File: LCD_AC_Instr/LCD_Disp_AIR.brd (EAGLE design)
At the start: 40.3 x 49.5 mm, 12 parts, among them J1 CON_HEADER_1X02-PTH, SW1 ENCODER_SW1-PEC12

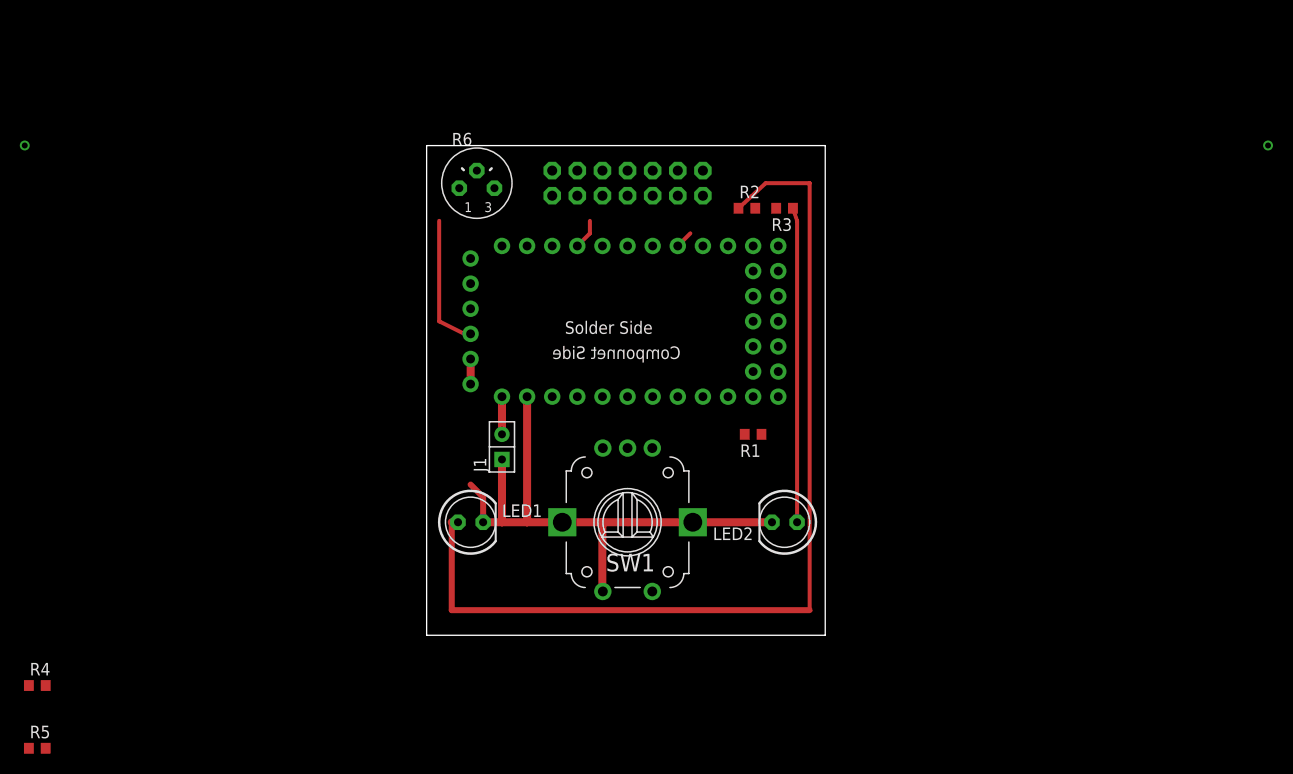
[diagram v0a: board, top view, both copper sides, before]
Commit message: finished design of PCB and uploaded to OSH PCB
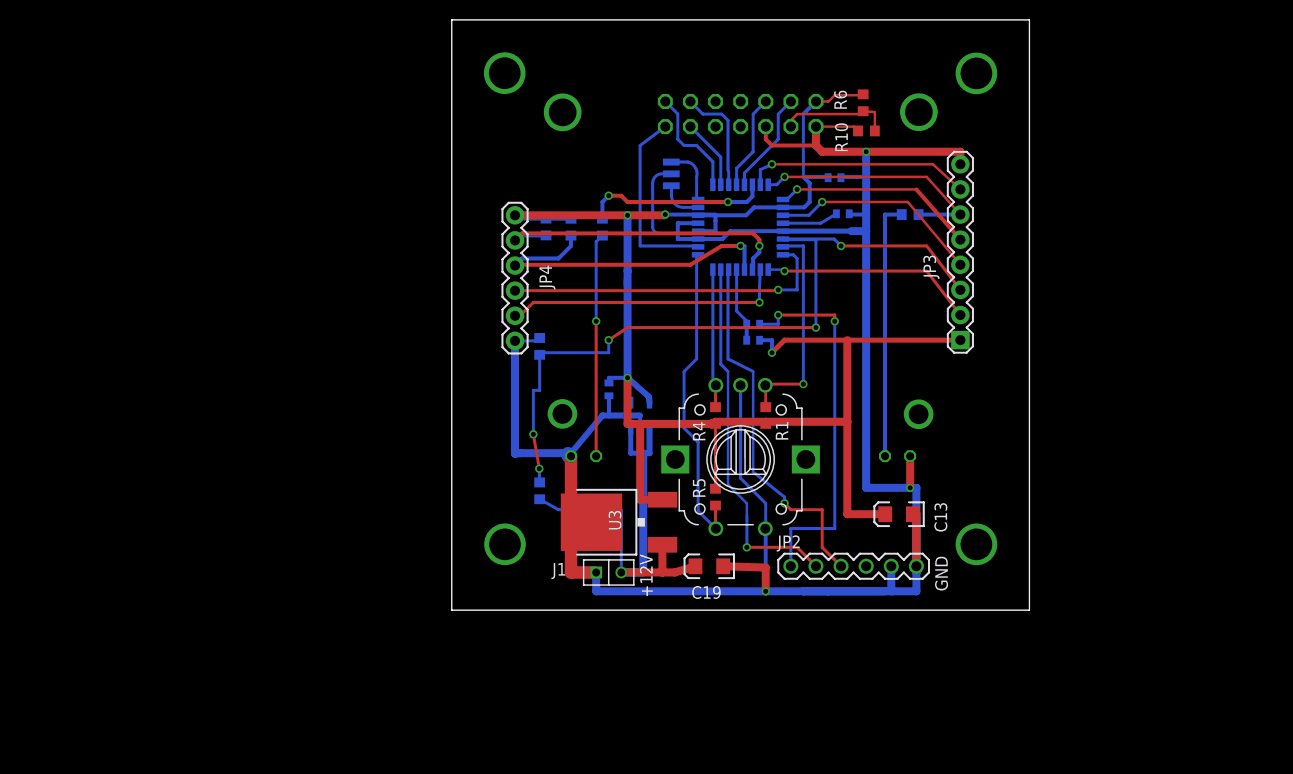
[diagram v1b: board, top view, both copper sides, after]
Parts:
- removed JP1: (no value), pinhead:2X07
- removed U$1: ARDUINO_PRO_MONI_DEEK_ROBOT, Arduino_Pro_FP:DEEK_ARDUINO_PR_MINI
- added C1, C10, C2, C3: 0.1uF, SparkFun:C0402
- added C13, C19: 10uF, SparkFun:EIA3216
- added JP2: 5V UART, SparkFun:1X06
- added JP3: 1, SparkFun-Connectors:1X08
- added JP4: 1, SparkFun-Connectors:1X06
- added LCD: LCD, pinhead:2X07
- added Q1: 16MHz, SparkFun:RESONATOR-SMD
- added R10, R11: 10K, dp_devices:R603
- added R12: 5K, dp_devices:R603
- added R7, R8: 1k, dp_devices:R603
- added R9: 10K, SparkFun:C0402
- added U1: ATMEGA328P, SparkFun:TQFP32-08
- added U2: 5V, SparkFun:SOT23-5
- added U3: +5V, wifi_WX:DPACK
- J1: value CON_HEADER_1X02-PTH -> 12V input
- R6: value (none) -> 10K; device pot:RJ6 -> dp_devices:R603
- moved R4 73.8 mm to (29.2, 21.0), turned to 90 degrees
- moved R5 73.1 mm to (29.2, 12.7), turned to 90 degrees
- moved R6 39.9 mm to (44.1, 52.6), turned to 90 degrees
- moved J1 16.7 mm to (18.4, 5.08), turned to 0 degrees
- moved R2 14.7 mm to (17.8, 40.0), flipped to the bottom, turned to 90 degrees
- moved LED1 13.2 mm to (15.9, 16.8), flipped to the bottom
- moved LED2 13.2 mm to (47.6, 16.8), flipped to the bottom
- moved SW1 13.1 mm to (31.8, 16.5)
- moved R3 12.7 mm to (48.9, 41.3), flipped to the bottom
- moved R1 2.29 mm to (34.3, 21.0), turned to 270 degrees
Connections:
- removed net +12V: J1.2, U$1.RAW
- removed net CONTRAST: JP1.3, R6.S
- removed net N$1: JP1.11, U$1.4
- removed net N$10: R4.2, SW1.A, U$1.2
- removed net N$11: U$1.A3
- removed net N$12: U$1.A0
- removed net N$3: JP1.12, U$1.5
- removed net N$4: JP1.6, U$1.9
- removed net N$7: R1.1, SW1.B, U$1.10
- removed net VCC_5V: JP1.2, R1.2, R4.1, R5.2, R6.E, U$1.VCC_2
- new net 12V_INPUT: C19.A, J1.2, R11.2, U2.1, U2.3, U3.1
- new net 5V: C10.1, C13.A, C3.2, JP3.1, JP4.1, LCD.2, R1.2, R4.1, R5.2, R6.2, R7.1, R8.1, R9.2, U1.18, U1.4, U1.6, U2.5, U3.3
- new net A0_PC0: R1.1, SW1.A, U1.23
- new net A1_PC1: JP4.4, U1.24
- new net A2_PC2: JP3.2, U1.25
- new net A3_PC3: JP4.5, U1.26
- new net A4_PC4: JP4.2, R7.2, U1.27
- new net A5_PC5: JP4.3, R8.2, U1.28
- new net ADC6: JP3.4, U1.19
- new net ADC7: JP3.3, R11.1, R12.2, U1.22
- new net AREF: C1.2, U1.20
- new net D10_PB2: R2.2, U1.14
- new net D11_PB3_MOSI: JP3.7, U1.15
- new net D12_PB4_MISO: JP3.6, R3.2, U1.16
- new net D13_PB5_SCK: JP3.5, U1.17
- new net D2_PD2: R4.2, SW1.B, U1.32
- new net D3_PD3: R5.1, SW1.P2, U1.1
- new net D4_PD4: LCD.13, U1.2
- new net D5_PD5: LCD.14, U1.9
- new net D6_PD6: LCD.11, U1.10
- new net D7_PD7: LCD.12, U1.11
- new net D8_PB0: LCD.6, U1.12
- new net D9_PB1: LCD.4, U1.13
- new net RESET: C2.1, R9.1, U1.29
- new net RXI: JP2.3, U1.30
- new net TXO: JP2.2, U1.31
- net GND: now also C1.1, C10.2, C13.C, C19.C, C3.1, JP2.5, JP2.6, JP3.8, JP4.6, LCD.1, LCD.5, Q1.2, R10.1, R12.1, SW1.P1, U1.21, U1.3, U1.5, U2.2, U3.4; no longer JP1.1, JP1.5, R6.A, SW1.P2, U$1.GND, U$1.GND_2, U$1.GND_3, U$1.GND_4
- net N$2: now also LCD.3, R10.2, R6.1; no longer JP1.13, U$1.6
- net N$5: now also Q1.1, U1.8; no longer JP1.4, U$1.8
- net N$6: now also C2.2, JP2.1; no longer R5.1, SW1.P1, U$1.3
- net N$9: now also Q1.3, U1.7; no longer JP1.14, U$1.7
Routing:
- net GND: track 65.2 -> 247.9 mm, vias 0 -> 3
- net 5V: track 0.00 -> 171.4 mm, vias 0 -> 4
- net ADC7: track 0.00 -> 76.1 mm, vias 0 -> 5
- net N$13: track 97.1 -> 22.6 mm, vias 0 -> 1
- net 12V_INPUT: track 0.00 -> 46.5 mm
- net N$6: track 0.00 -> 38.9 mm, vias 0 -> 2
- net RXI: track 0.00 -> 37.4 mm, vias 0 -> 1
- net TXO: track 0.00 -> 37.0 mm, vias 0 -> 1
- net A5_PC5: track 0.00 -> 33.9 mm, vias 0 -> 1
- net A1_PC1: track 0.00 -> 33.3 mm, vias 0 -> 1
- net D3_PD3: track 0.00 -> 32.1 mm
- net A4_PC4: track 0.00 -> 31.9 mm, vias 0 -> 1
- net A3_PC3: track 0.00 -> 28.6 mm, vias 0 -> 1
- net D12_PB4_MISO: track 0.00 -> 25.7 mm, vias 0 -> 1
- net A0_PC0: track 0.00 -> 22.9 mm, vias 0 -> 1
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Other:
- board size 40.3 x 49.5 mm -> 58.4 x 59.7 mm
- board text added: "+12V"
- board text added: "GND"

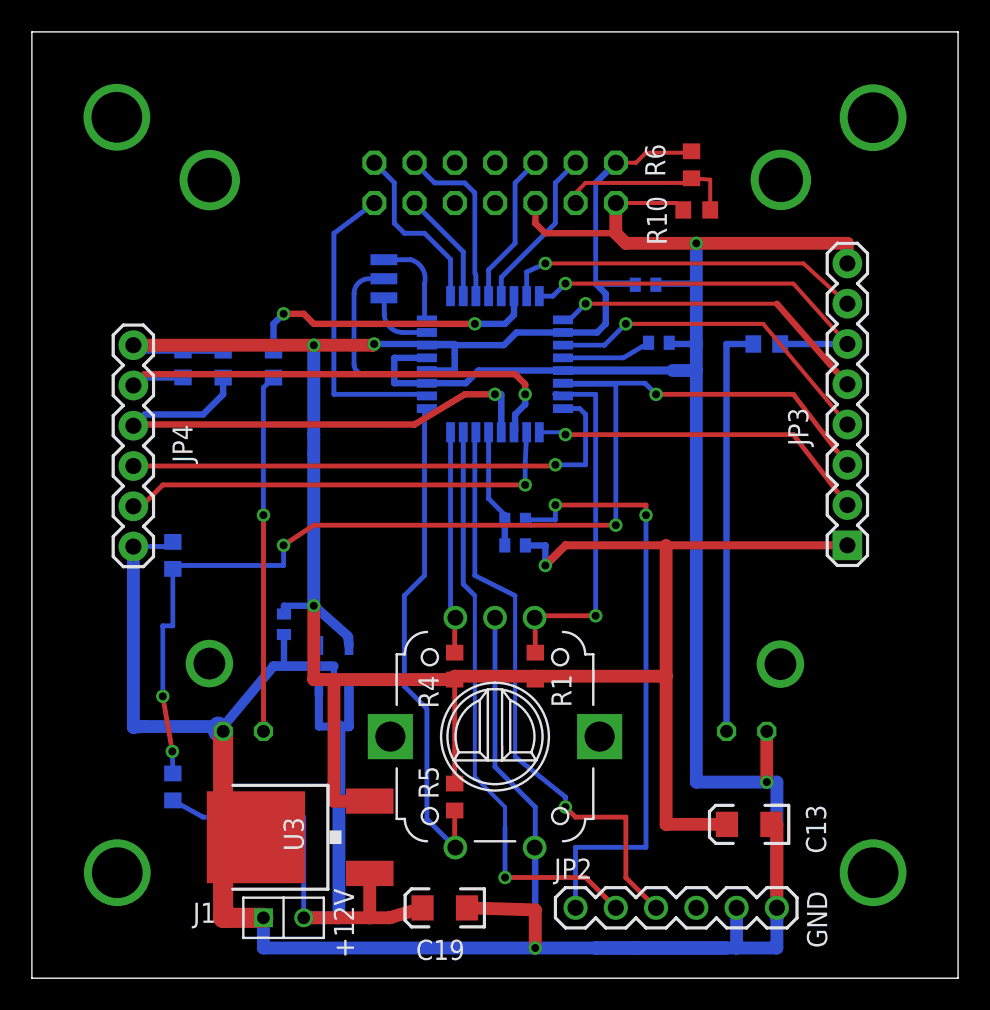
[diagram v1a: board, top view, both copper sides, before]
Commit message: labeled connectors
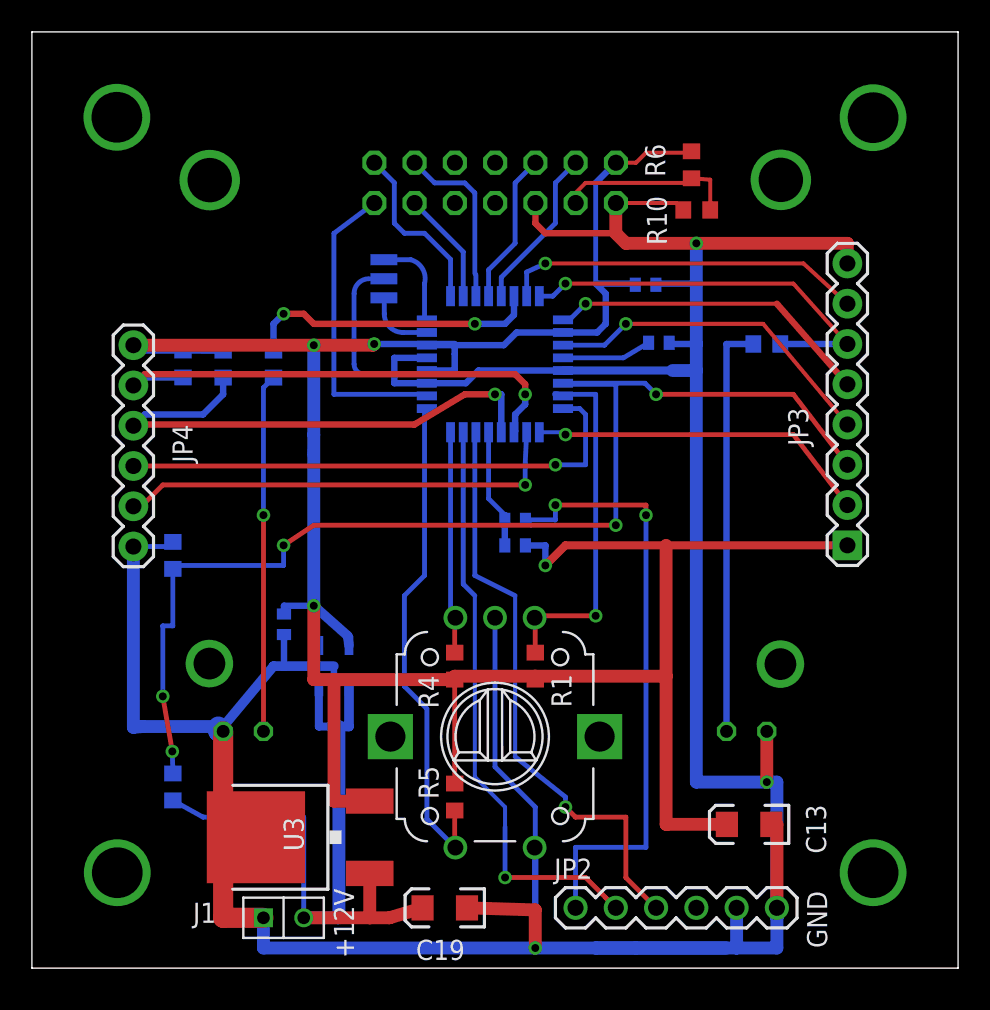
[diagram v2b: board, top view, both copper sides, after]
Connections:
- net A4_PC4 renamed A4_PC4_SDA
- net A5_PC5 renamed A5_PC5_SCL
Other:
- board size 58.4 x 59.7 mm -> 58.4 x 59.1 mm
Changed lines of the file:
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@@
 <wire x1="45.3898" y1="47.8536" x2="50.6476" y2="47.8536" width="0.0254" layer="199"/>
 <wire x1="2.54" y1="60.96" x2="60.96" y2="60.96" width="0.0254" layer="20"/>
-<wire x1="60.96" y1="60.96" x2="60.96" y2="1.27" width="0.0254" layer="20"/>
-<wire x1="60.96" y1="1.27" x2="2.54" y2="1.27" width="0.0254" layer="20"/>
-<wire x1="2.54" y1="1.27" x2="2.54" y2="60.96" width="0.0254" layer="20"/>
+<wire x1="60.96" y1="60.96" x2="60.96" y2="1.905" width="0.0254" layer="20"/>
+<wire x1="60.96" y1="1.905" x2="2.54" y2="1.905" width="0.0254" layer="20"/>
+<wire x1="2.54" y1="1.905" x2="2.54" y2="60.96" width="0.0254" layer="20"/>
 <wire x1="11.5062" y1="8.6106" x2="51.9938" y2="8.6106" width="0.0254" layer="199"/>
 <text x="22.86" y="2.54" size="1.27" layer="21" rot="R90">+12V </text>
@@
 <wire x1="32.385" y1="7.62" x2="32.385" y2="10.795" width="0.3048" layer="16"/>
 </signal>
-<signal name="A5_PC5">
+<signal name="A5_PC5_SCL">
 <contactref element="U1" pad="28"/>
 <contactref element="R8" pad="2"/>
@@
 <wire x1="9.652" y1="36.83" x2="8.9408" y2="36.1188" width="0.4064" layer="16"/>
 </signal>
-<signal name="A4_PC4">
+<signal name="A4_PC4_SDA">
 <contactref element="U1" pad="27"/>
 <contactref element="R7" pad="2"/>

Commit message: Revised to rev 0.1
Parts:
- removed U2: 5V, SparkFun:SOT23-5
- added C4, C5, C6, C8, C9: 0.1uF, SparkFun:0805
- added C7: 10uF, SparkFun:EIA3216
- added F1: (no value), dp_devices:PTC0805
- added IC3: TC10553.3V, 1AA_Stofer:SOT23-5
- C1, C10, C2, C3: device SparkFun:C0402 -> SparkFun:0805
- C19: device SparkFun:EIA3216 -> SparkFun:EIA7343
- R10: value 10K -> 120
- R11: value 10K -> 14K
- R12: value 5K -> 6.8K
- R2, R3: value 330 -> 470
- R6: value 10K -> (none)
- R9: device SparkFun:C0402 -> SparkFun:0603
- U1: value ATMEGA328P -> ATMEGA328P-AU(R)
- U3: value +5V -> 78M05
- moved R12 30.5 mm to (33.0, 6.35), turned to 90 degrees
- moved R11 17.9 mm to (27.9, 6.35)
- moved C10 13.0 mm to (21.5, 36.2), turned to 180 degrees
- moved R3 10.5 mm to (46.4, 31.1), turned to 90 degrees
- moved R1 7.10 mm to (27.3, 22.2)
- moved R4 7.10 mm to (36.2, 22.2)
- moved R5 5.68 mm to (24.1, 10.2), flipped to the bottom, turned to 0 degrees
- moved JP3 2.84 mm to (55.2, 26.0)
- moved C19 2.01 mm to (30.5, 6.34)
- moved C13 1.61 mm to (46.2, 10.6), flipped to the bottom, turned to 0 degrees
- moved J1 0.71 mm to (17.8, 5.40)
- moved JP4 0.69 mm to (8.26, 41.3)
- moved C2 0.63 mm to (33.0, 30.8)
- flipped SW1 to the bottom
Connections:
- removed net D2_PD2: R4.2, SW1.B, U1.32
- removed net D3_PD3: R5.1, SW1.P2, U1.1
- new net D2_PD2(INT0): C4.2, R1.1, SW1.A, U1.32
- new net D3_PD3(INT1): C6.2, R5.1, SW1.P1, U1.1
- new net N$11: F1.1, J1.2
- new net V3_3V: C7.A, C8.1, IC3.5, JP4.5
- net 12V_INPUT: now also F1.2; no longer J1.2, U2.1, U2.3
- net 5V: now also IC3.1, IC3.3; no longer U2.5
- net A0_PC0: now also C5.2, R4.2, SW1.B; no longer R1.1, SW1.A
- net A3_PC3: now also R3.2; no longer JP4.5
- net ADC7: now also C9.1; no longer JP3.3
- net D12_PB4_MISO: no longer R3.2
- net GND: now also C4.1, C5.1, C6.1, C7.C, C8.2, C9.2, IC3.2, SW1.P2; no longer SW1.P1, U2.2
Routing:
- net D3_PD3(INT1): track 0.00 -> 38.0 mm
- net 5V: track 171.4 -> 209.0 mm, vias 4 -> 6
- net 12V_INPUT: track 46.5 -> 11.1 mm, vias 0 -> 1
- net D3_PD3: track 32.1 -> 0.00 mm
- net ADC7: track 76.1 -> 46.3 mm, vias 5 -> 0
- net V3_3V: track 0.00 -> 28.7 mm, vias 0 -> 1
- net D2_PD2(INT0): track 0.00 -> 16.4 mm
- net D2_PD2: track 14.2 -> 0.00 mm
- net GND: track 247.9 -> 260.8 mm
- net N$15: track 26.1 -> 15.1 mm
- net A3_PC3: track 28.6 -> 18.3 mm, vias 1 -> 2
- net N$11: track 0.00 -> 2.71 mm
- net D11_PB3_MOSI: track 22.9 -> 25.2 mm
- net D13_PB5_SCK: track 20.7 -> 22.8 mm
- net D12_PB4_MISO: track 25.7 -> 23.6 mm
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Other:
- board size 58.4 x 59.1 mm -> 58.4 x 58.4 mm
- board text added: "1"
- board text added: "AIR_LCDuino rev 0.1"
- board text added: "RV-Builders Products"
